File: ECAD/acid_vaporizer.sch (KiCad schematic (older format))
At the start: 62 parts, among them J1 Screw_Terminal_01x02, J2 Screw_Terminal_01x02, J3 Screw_Terminal_01x01, J4 Screw_Terminal_01x01, J5 Conn_ARM_JTAG_SWD_10, J6 Screw_Terminal_01x02, J7 Conn_01x02_Male, Q1 BTA16-800BW, Q2 BC817, Q3 BC817, Q4 BC817, U1 OPA333xxD, U2 STM32F030F4Px, U3 AMS1117-3.3, U4 OPA333xxD, U5 DS18B20, U6 74HC164, U7 MOC3063M, U8 E30281, Y1 8MHz

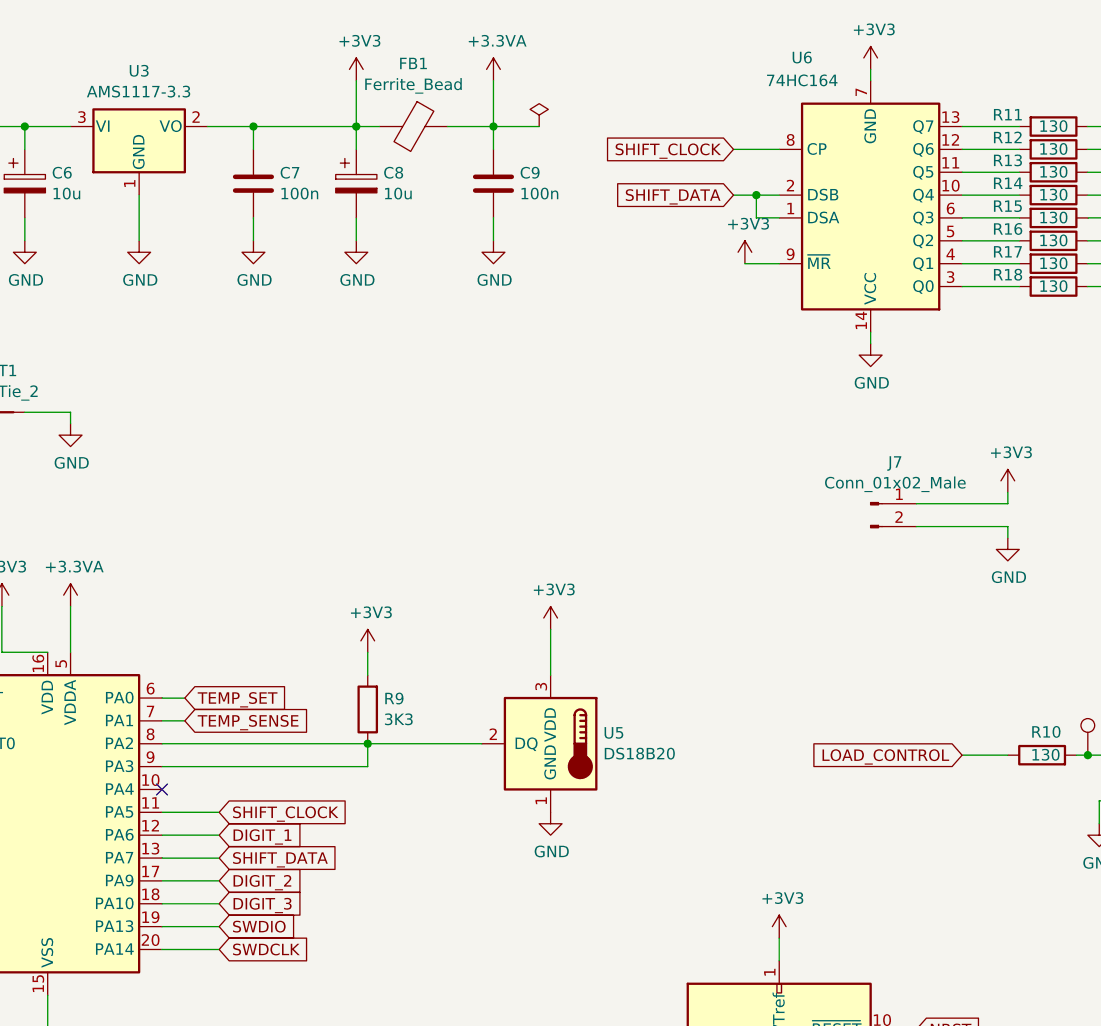
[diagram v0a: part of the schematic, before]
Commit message: Schematic and PCB: replasce DS18B20 by TMP36
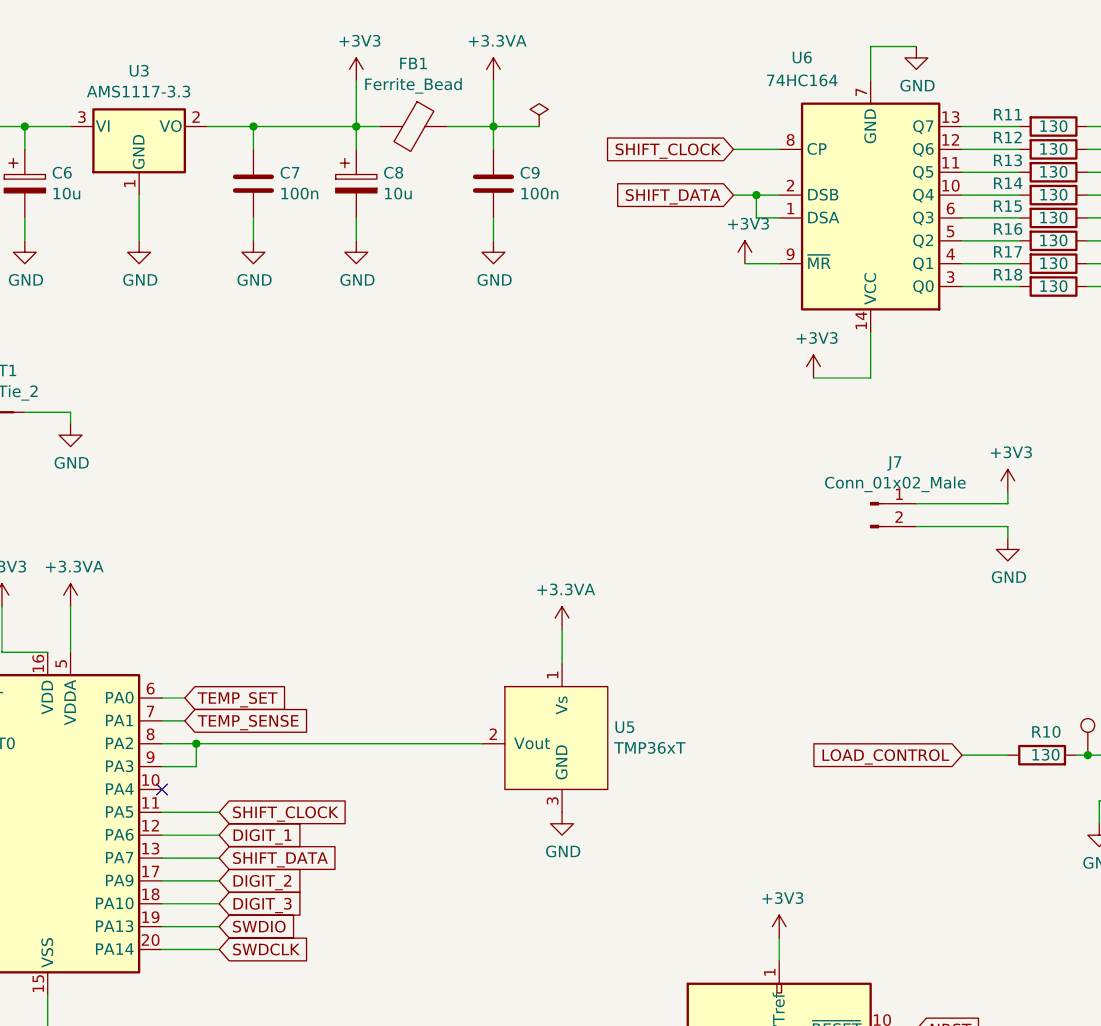
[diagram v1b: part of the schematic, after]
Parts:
- removed R9: 3K3, Resistor_SMD:R_0805_2012Metric_Pad1.15x1.40mm_HandSolder, symbol Device:R
- removed U5: DS18B20, Package_TO_SOT_THT:TO-92_Inline, symbol Sensor_Temperature:DS18B20
- added U5: TMP36xT, Package_TO_SOT_THT:TO-92, symbol MiscComponents:TMP36xT
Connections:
- net +3.3VA: now also U5.1 (Vs)
- net +3V3: now also U6.14 (VCC); no longer U6.7 (GND)
- net GND: now also U6.7 (GND), U5.3 (GND); no longer U6.14 (VCC)
- net at U2.8 (PA2), U2.9 (PA3): now also U5.2 (Vout)
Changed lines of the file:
@@
-$EndComp
-$Comp
-L Sensor_Temperature:DS18B20 U5
-U 1 1 5F6CD638
-P 5750 3700
-F 0 "U5" H 5520 3746 50  0000 R CNN
-F 1 "DS18B20" H 5520 3655 50  0000 R CNN
-F 2 "Package_TO_SOT_THT:TO-92_Inline" H 4750 3450 50  0001 C CNN
-F 3 "http://datasheets.maximintegrated.com/en/ds/DS18B20.pdf" H 5600 3950 50  0001 C CNN
-	1    5750 3700
-	-1   0    0    -1
 $EndComp
 $Comp
@@
 	1    0    0    -1
 $EndComp
-Connection ~ 4950 3700
-$Comp
-L power:+3V3 #PWR0124
-U 1 1 5F7AD082
-P 5750 3200
-F 0 "#PWR0124" H 5750 3050 50  0001 C CNN
-F 1 "+3V3" H 5765 3373 50  0000 C CNN
-F 2 "" H 5750 3200 50  0001 C CNN
-F 3 "" H 5750 3200 50  0001 C CNN
-	1    5750 3200
-	1    0    0    -1
-$EndComp
 $Comp
 L power:GND #PWR0125
 U 1 1 5F7AD992
-P 5750 4000
-F 0 "#PWR0125" H 5750 3750 50  0001 C CNN
-F 1 "GND" H 5755 3827 50  0000 C CNN
-F 2 "" H 5750 4000 50  0001 C CNN
-F 3 "" H 5750 4000 50  0001 C CNN
-	1    5750 4000
-	1    0    0    -1
-$EndComp
-Wire Wire Line
-	5750 3400 5750 3200
+P 5800 4000
+F 0 "#PWR0125" H 5800 3750 50  0001 C CNN
+F 1 "GND" H 5805 3827 50  0000 C CNN
+F 2 "" H 5800 4000 50  0001 C CNN
+F 3 "" H 5800 4000 50  0001 C CNN
+	1    5800 4000
+	1    0    0    -1
+$EndComp
 $Comp
 L power:+3V3 #PWR0126
@@
 Wire Wire Line
 	2800 3100 2800 3200
-Wire Wire Line
-	4950 3700 5450 3700
-$Comp
-L Device:R R9
-U 1 1 5F7BC0F2
-P 4950 3550
-F 0 "R9" H 4880 3504 50  0000 R CNN
-F 1 "3K3" H 4880 3595 50  0000 R CNN
-F 2 "Resistor_SMD:R_0805_2012Metric_Pad1.15x1.40mm_HandSolder" V 4880 3550 50  0001 C CNN
-F 3 "~" H 4950 3550 50  0001 C CNN
-	1    4950 3550
-	-1   0    0    1
-$EndComp
-$Comp
-L power:+3V3 #PWR0127
-U 1 1 5F7BC5A6
-P 4950 3300
-F 0 "#PWR0127" H 4950 3150 50  0001 C CNN
-F 1 "+3V3" H 4965 3473 50  0000 C CNN
-F 2 "" H 4950 3300 50  0001 C CNN
-F 3 "" H 4950 3300 50  0001 C CNN
-	1    4950 3300
-	1    0    0    -1
-$EndComp
-Wire Wire Line
-	4950 3300 4950 3400
 $Comp
 L Device:R R4
@@
 L power:GND #PWR0138
 U 1 1 5F7BDC69
-P 7150 1950
-F 0 "#PWR0138" H 7150 1700 50  0001 C CNN
-F 1 "GND" H 7155 1777 50  0000 C CNN
-F 2 "" H 7150 1950 50  0001 C CNN
-F 3 "" H 7150 1950 50  0001 C CNN
-	1    7150 1950
-	1    0    0    -1
-$EndComp
-Wire Wire Line
-	7150 1950 7150 1900
+P 7350 650
+F 0 "#PWR0138" H 7350 400 50  0001 C CNN
+F 1 "GND" H 7355 477 50  0000 C CNN
+F 2 "" H 7350 650 50  0001 C CNN
+F 3 "" H 7350 650 50  0001 C CNN
+	1    7350 650
+	1    0    0    -1
+$EndComp
 $Comp
 L power:+3V3 #PWR0139
 U 1 1 5F7C330F
-P 7150 750
-F 0 "#PWR0139" H 7150 600 50  0001 C CNN
-F 1 "+3V3" H 7165 923 50  0000 C CNN
-F 2 "" H 7150 750 50  0001 C CNN
-F 3 "" H 7150 750 50  0001 C CNN
-	1    7150 750
-	1    0    0    -1
-$EndComp
-Wire Wire Line
-	7150 750  7150 800
+P 6900 2100
+F 0 "#PWR0139" H 6900 1950 50  0001 C CNN
+F 1 "+3V3" H 6915 2273 50  0000 C CNN
+F 2 "" H 6900 2100 50  0001 C CNN
+F 3 "" H 6900 2100 50  0001 C CNN
+	1    6900 2100
+	1    0    0    -1
+$EndComp
 Wire Wire Line
 	8150 4050 8150 3950
@@
 Wire Wire Line
 	9300 5650 9500 5650
-Wire Wire Line
-	4050 3700 4950 3700
-Wire Wire Line
-	4050 3800 4950 3800
-Wire Wire Line
-	4950 3800 4950 3700
 Wire Wire Line
 	4150 3500 4050 3500
@@
 Wire Wire Line
 	6600 1600 6750 1600
+Wire Wire Line
+	6900 2100 7150 2100
+Wire Wire Line
+	7150 2100 7150 1900
+Wire Wire Line
+	7150 650  7350 650
+Wire Wire Line
+	7150 650  7150 800
+Wire Wire Line
+	4050 3700 4200 3700
+$Comp
+L MiscComponents:TMP36xT U5
+U 1 1 606196FF
+P 5800 3700
+F 0 "U5" H 6028 3771 50  0000 L CNN
+F 1 "TMP36xT" H 6028 3680 50  0000 L CNN
+F 2 "Package_TO_SOT_THT:TO-92" H 5800 4150 50  0001 C CNN
+F 3 "" H 5800 4150 50  0001 C CNN
+	1    5800 3700
+	1    0    0    -1
+$EndComp
+$Comp
+L power:+3.3VA #PWR0124
+U 1 1 6062530E
+P 5800 3200
+F 0 "#PWR0124" H 5800 3050 50  0001 C CNN
+F 1 "+3.3VA" H 5815 3373 50  0000 C CNN
+F 2 "" H 5800 3200 50  0001 C CNN
+F 3 "" H 5800 3200 50  0001 C CNN
+	1    5800 3200
+	1    0    0    -1
+$EndComp
+Wire Wire Line
+	5800 3200 5800 3350
+Wire Wire Line
+	4050 3800 4200 3800
+Wire Wire Line
+	4200 3800 4200 3700
+Connection ~ 4200 3700
+Wire Wire Line
+	4200 3700 5450 3700
 $EndSCHEMATC
